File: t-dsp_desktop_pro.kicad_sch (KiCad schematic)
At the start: 192 parts, among them IC1 Logic Level Shifter - 74HCT2G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, J1 jumper, J10 JST-XH Connector -, J11 JST-XH Connector -, J12 RGB LED HEADEER, J13 Conn_01x02, J14 Conn_01x03, J15 Conn_01x01, J16 Conn_01x02, J17 Conn_02x04_Odd_Even, J18 Conn_02x02_Odd_Even, J19 Conn_01x01, J2 GROUND HEADER, J20 Conn_01x01, J3 jumper, J4 jumper, J5 jumper, J6 jumper, J7 jumper, J8 PJRAS2X1S01X, J9 PJRAS2X1S01X, Q1 DMG2307L-7, Q2 DMG2307L-7, SW1 SW_SPST, SW2 TL1105WF160Q - 3.15mm actuator, SW3 SW_SPST, SW4 SW_SPST, SW5 RotaryEncoder_Switch_MP, SW6 TL1105WF160Q - 3.15mm actuator, SW7 TL1105WF160Q - 3.15mm actuator, SW8 TL1105WF160Q - 3.15mm actuator, T108 Tab, T109 Tab, T110 Tab, T111 Tab, U1 Teensy 4.1 - DEVKIT, U10 TPD4E02B04DQA, U2 ESP32-DevKitC - DEVKIT, U3 Power Mux & Protect - TPS2116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, U4 Optoisolators - H11L1SM - 6-S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, U5 Dual Buffer - SN74LVC2G125DCTR, U6 Dual Buffer - SN74LVC2G125DCTR, U7 Dual Buffer - SN74LVC2G125DCTR, U8 Dual Buffer - SN74LVC2G125DCTR, U9 Dual Buffer - 74HCT2G17GW,125

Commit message: v0.81: Fix CI release, localize 3D models, update README with render gallery
- Fix workflow: add gh release create before upload (tag != release)
- Fix ZIP filename: remove empty %r board revision from output name
- Localize 3D model paths for U10, C15, JST connectors to ${KIPRJMOD}
- Add project-local footprints for C_1206 and JST_XH_S2B-XH-A
- Trim SMD 3D renders from 8 to 4 views (top, bottom, top_iso, bottom_iso)
- Update gallery.html to handle different view counts per set
- Update README: Blender render thumbnails linking to gallery, fix IC table,
  add new components (U10, IC1, D5, Q1/Q2), update project files table
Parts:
- C1, C29, C30: Digikey 13-CC1206MKX5R5BB107CT-ND -> (none); Manufacturer YAGEO -> (none); Manufacturer_Part_Number CC1206MKX5R5BB107 -> (none)
- C10, C11, C2, C22, C24, C25, C26, C3, C4, C5: Manufacturer Kyocera AVX -> (none); Manufacturer_Part_Number 08055C104M4T4A -> (none)
- C15: footprint Capacitor_SMD:C_1206_3216Metric_Pad1.33x1.80mm_HandSolder -> project_fp:C_1206_3216Metric_Pad1.33x1.80mm_HandSolder
- C16, C17, C18, C19, C20, C21: Manufacturer KEMET -> (none); Manufacturer_Part_Number C0805C104K5RAC7411 -> (none)
- CC1, CC2, R29, R30: Digikey - -> (none); Manufacturer - -> (none); Manufacturer_Part_Number 0805W8F5101T5E -> (none)
- D2: Manufacturer Panjit -> (none); Manufacturer_Part_Number 1N4148W_R1_00001 -> (none)
- D5: LCSC TYPE (none) -> SMD; Manufacturer_Name Texas Instruments -> (none); Manufacturer_Part_Number TPD1E10B06DPYT -> (none); Mouser Part Number 595-TPD1E10B06DPYT -> (none); Mouser Price/Stock https://www.mouser.co.uk/ProductDetail/Texas-Instruments/TP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 -> (none)
- ESP_I1, MIDI_IO1, TDM1, TDM2, USB_DEVICE_1, USB_HOST_1: Digikey - -> (none); Manufacturer - -> (none); Manufacturer_Part_Number - -> (none)
- G1, G2, ILI_LED1, ILI_LED2, J1, J3, J4, J5, J6, J7, MIDI_OT1, MIDI_OT2: Digikey - -> (none); Manufacturer - -> (none); Manufacturer_Part_Number ~jumper -> (none)
- HPTRS1, HPTRS2: Manufacturer Switchcraft -> (none); Manufacturer_Part_Number 35RAPC3BH3 -> (none)
- IC1: Manufacturer_Name Nexperia -> (none); Manufacturer_Part_Number 74HCT2G125DC,125 -> (none)
- J10, J11: value JST-XH Connector - -> JST-XH Connector; footprint Connector_JST:JST_XH_S2B-XH-A_1x02_P2.50mm_Horizontal -> project_fp:JST_XH_S2B-XH-A_1x02_P2.50mm_Horizontal; Manufacturer_Part_Number JST-XH -> (none)
- MIDI_IN_1, MIDI_OUT_1: Manufacturer Switchcraft -> (none); Manufacturer_Part_Number 35RAPC4BHN2 -> (none)
- PU_EN108: TAC5212EVM n/a -> (none)
- PWR1, PWR2, PWR3: Manufacturer_Part_Number through-hole -> (none)
- Q1, Q2: Manufacturer_Name Diodes Incorporated -> (none); Manufacturer_Part_Number DMG2307L-7 -> (none); Mouser Part Number 621-DMG2307L-7 -> (none); Mouser Price/Stock https://www.mouser.co.uk/ProductDetail/Diodes-Incorporated/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 -> (none); Package / Case (none) -> SOT-23
- R11, R20, R21: Digikey ERJ-PA2F2211X-ND -> (none); Manufacturer YAGEO -> (none); Manufacturer_Part_Number RC0805DR-072K2L -> (none)
- R28: Digikey - -> (none); Manufacturer - -> (none); Manufacturer_Part_Number ERJ-PB6D5101V -> (none)
- R32, R34, R36, R37, R38, R39: Manufacturer Bourns -> (none); Manufacturer_Part_Number CR0805-FX-2200ELF -> (none)
- R33: Manufacturer Panasonic -> (none); Manufacturer_Part_Number ERA-6AED152V -> (none)
- TR1: Manufacturer Everlight Electronics -> (none); Manufacturer_Part_Number FCR6842032R -> (none)
- TT1: Manufacturer Everlight Electronics -> (none); Manufacturer_Part_Number FCR6842032T -> (none)
- U1: Manufacturer PJRC -> (none); Manufacturer_Part_Number ~Teensy4.1 -> (none)
- U10: footprint Package_SON:USON-10_2.5x1.0mm_P0.5mm -> project_fp:TPD4E02B04DQA; LCSC TYPE (none) -> SMD
- U4: Manufacturer_Part_Number H11L1SM -> (none)
- U9: Manufacturer_Part_Number 74HCT2G17GW,125 -> (none)
- USBA1: Digikey 380-1412-ND -> (none); Manufacturer Stewart Connector -> (none); Manufacturer_Part_Number SS-52100-001 -> (none)
- board_outline2: Digikey - -> (none); Manufacturer - -> (none); Manufacturer_Part_Number ~BOARD -> (none)

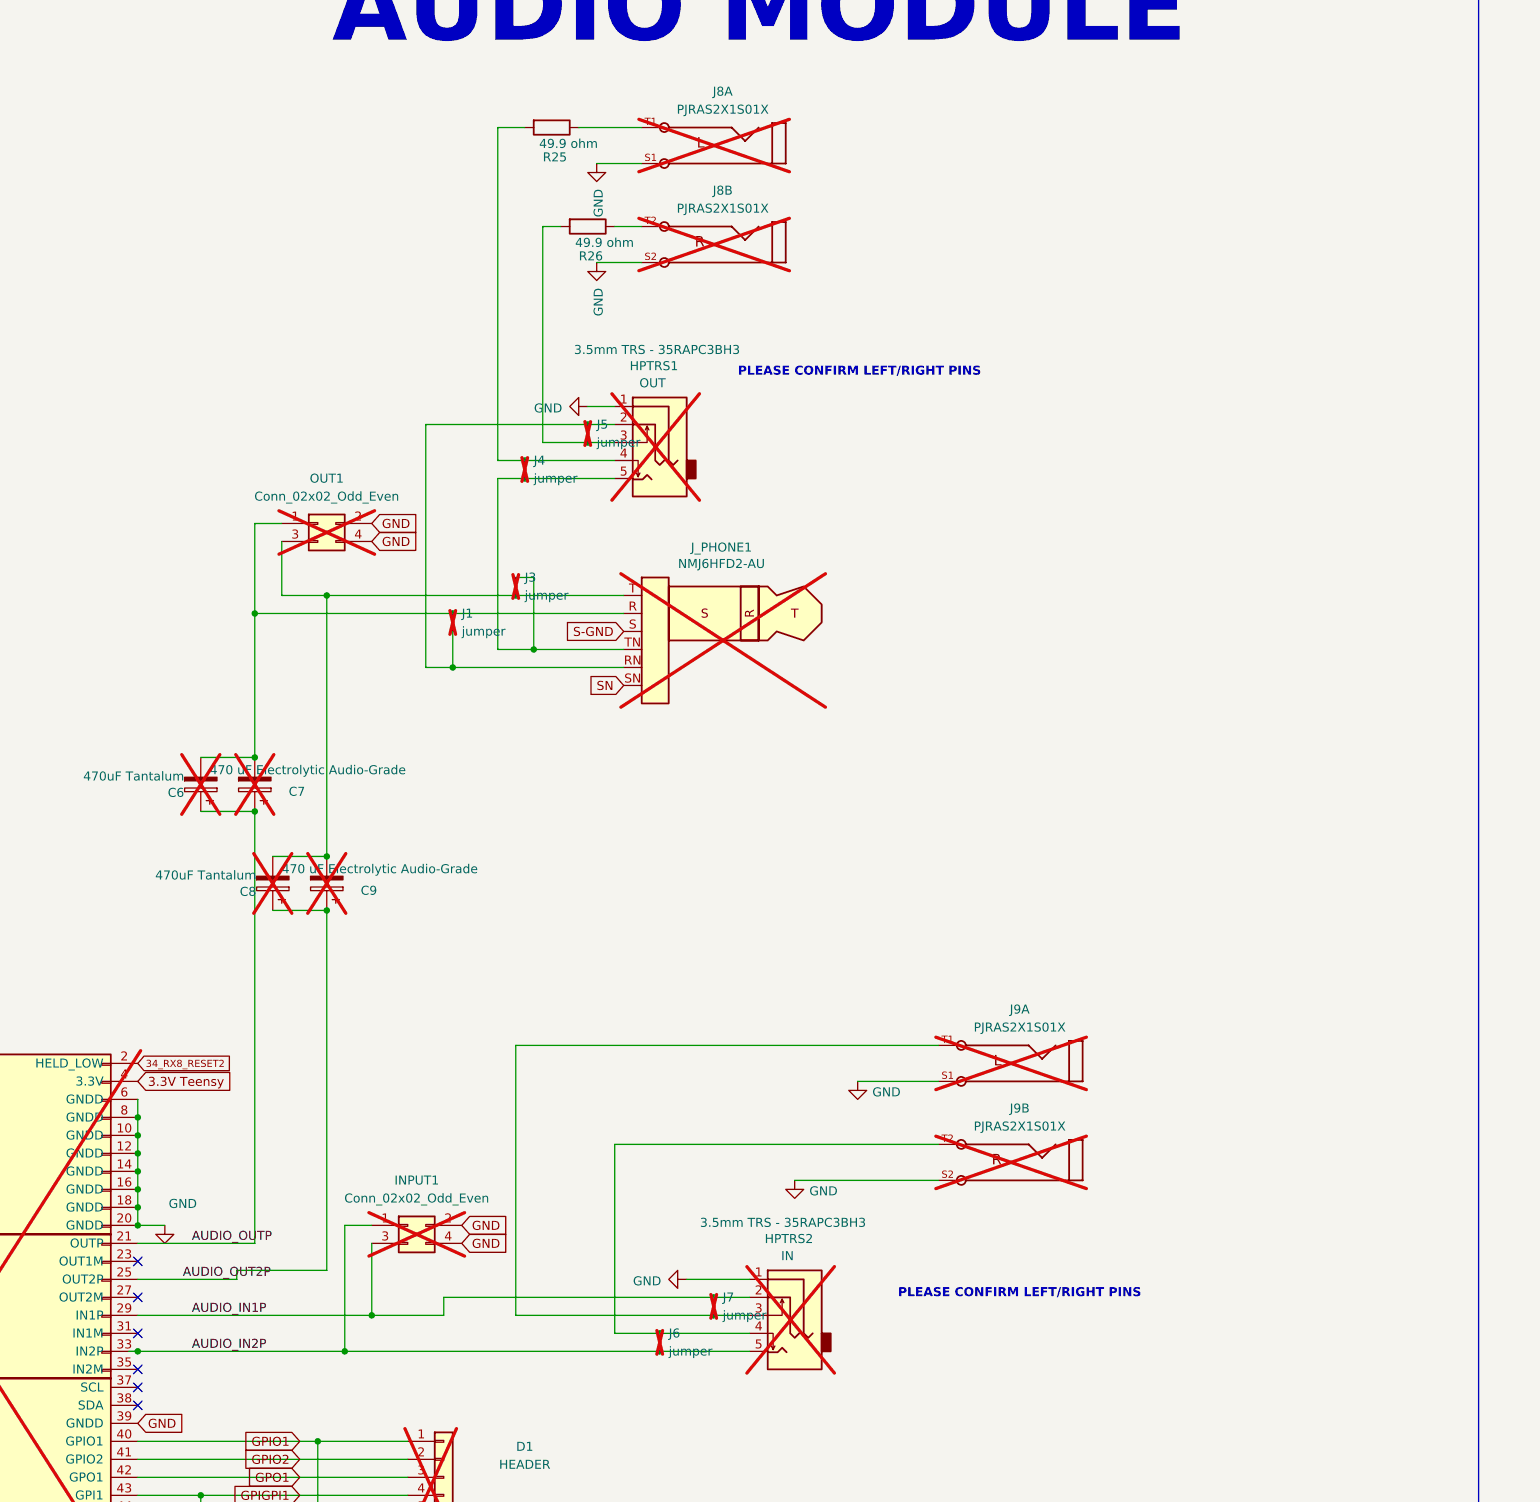
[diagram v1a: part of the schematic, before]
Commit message: v0.82: Fix audio output pin mapping and add PTC fuse footprint
- Correct L/R channel assignment: Left=OUT1, Right=OUT2
- Fix tip/ring polarity: +=tip, -=ring
- Add PTC resettable fuse (MF-LSMF300) footprint and 3D model
- Update workflow to include tag in manufacturing ZIP filename
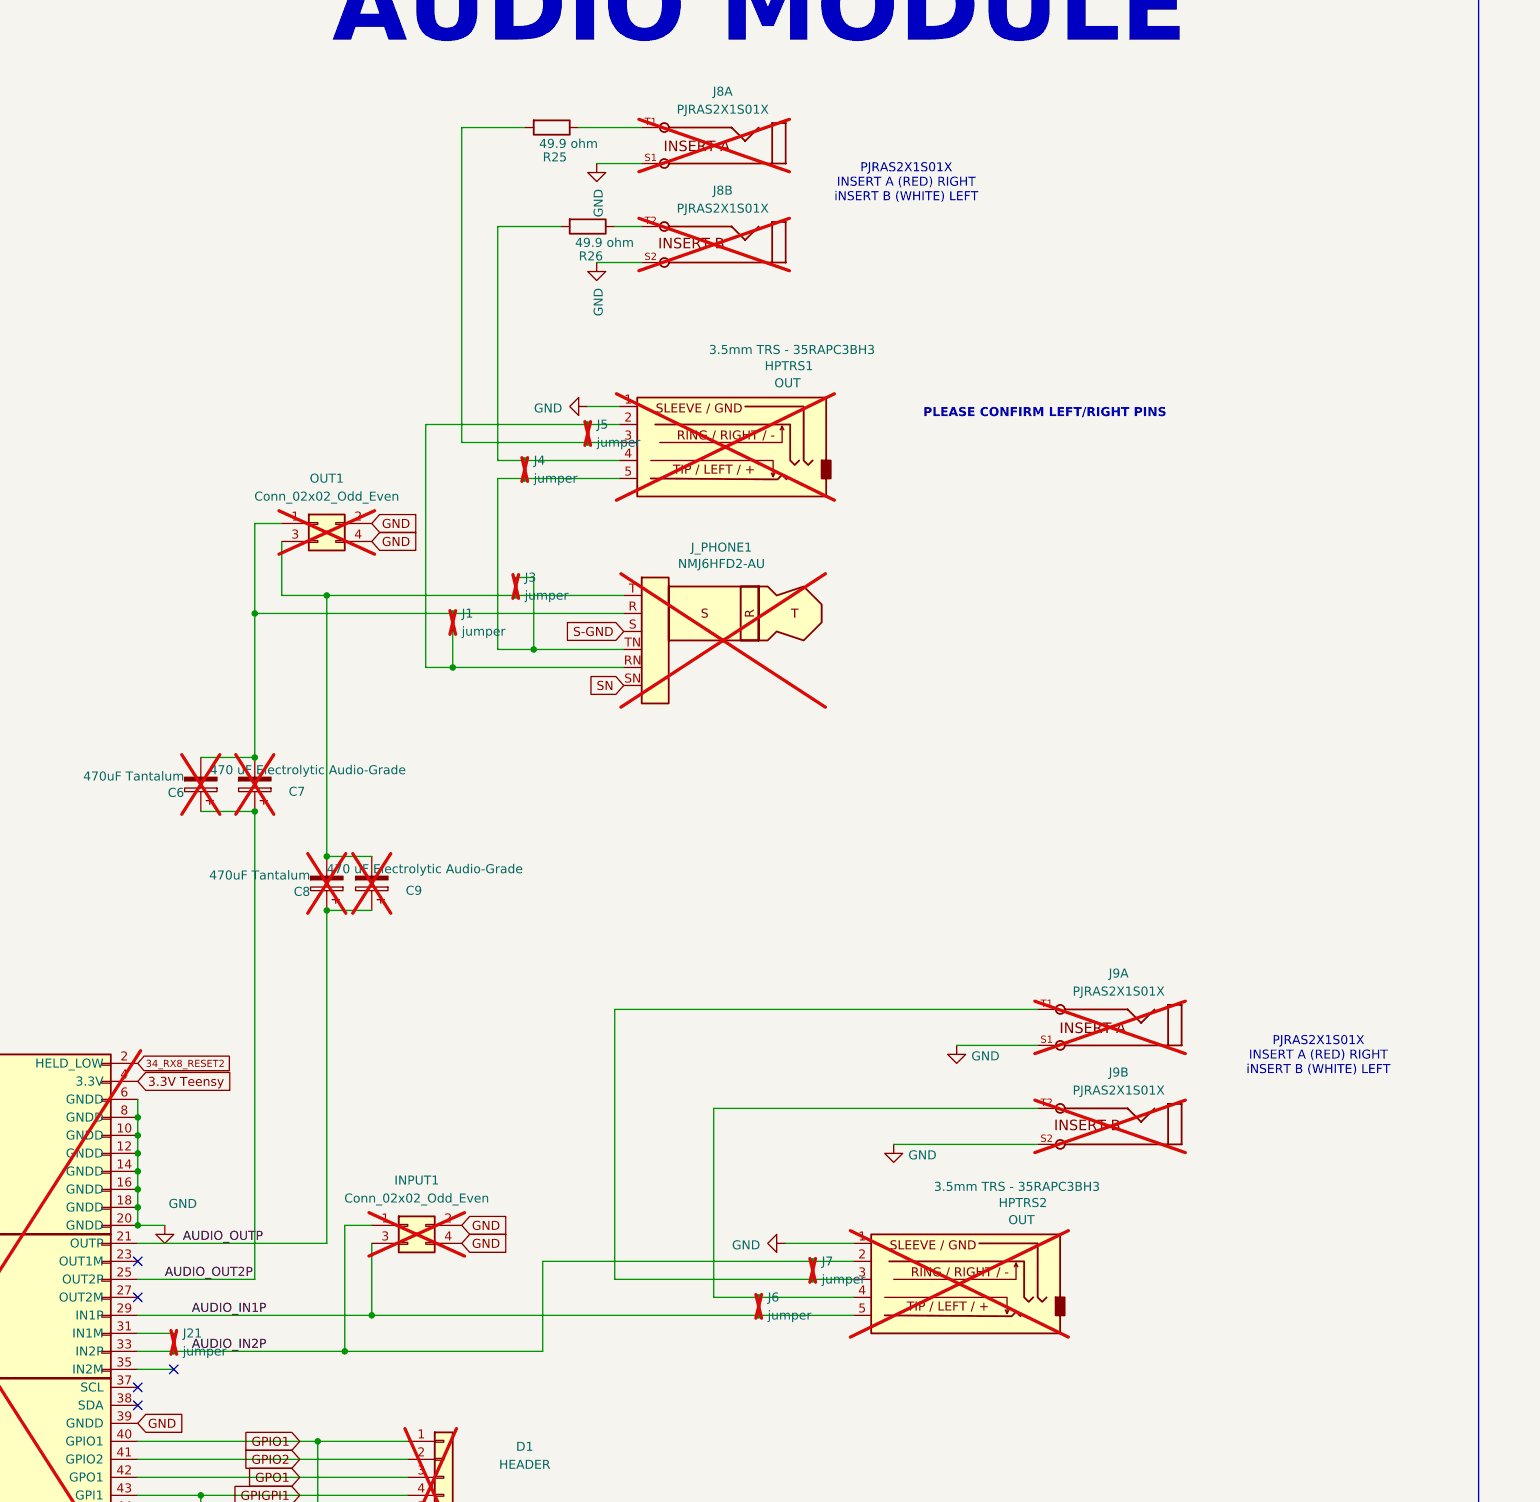
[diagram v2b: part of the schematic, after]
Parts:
- added J21: jumper, project_fp:jumper_slice, symbol project_sch:NetTie_2_mod
- HPTRS1: Manufacturer (none) -> Switchcraft; Manufacturer_Part_Number (none) -> 35RAPC3BH3
- HPTRS2: Label IN -> OUT; Manufacturer (none) -> Switchcraft; Manufacturer_Part_Number (none) -> 35RAPC3BH3
- J8, J9: Availability (none) -> In Stock; Check_prices (none) -> https://www.snapeda.com/parts/PJRAS2X1S01X/SWITCHCRAFT/view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; Description_1 (none) -> Connector, 2POS RA SHLD PHJK RE | Switchcraft PJRAS2X1S01X; MANUFACTURER (none) -> Switchcraft; MF (none) -> Switchcraft Inc.; MP (none) -> PJRAS2X1S01X; Package (none) -> None; Price (none) -> None; SnapEDA_Link (none) -> https://www.snapeda.com/parts/PJRAS2X1S01X/SWITCHCRAFT/view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
- J9: footprint project_fp:PJRAS2X1S01X_MOD2 -> PJRAS2X1S01X:PJRAS2X1S01X; Availability (none) -> In Stock; Check_prices (none) -> https://www.snapeda.com/parts/PJRAS2X1S01X/SWITCHCRAFT/view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; Description_1 (none) -> Connector, 2POS RA SHLD PHJK RE | Switchcraft PJRAS2X1S01X; MANUFACTURER (none) -> Switchcraft; MF (none) -> Switchcraft Inc.; MP (none) -> PJRAS2X1S01X; Package (none) -> None; Price (none) -> None; SnapEDA_Link (none) -> https://www.snapeda.com/parts/PJRAS2X1S01X/SWITCHCRAFT/view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
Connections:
- net AUDIO_IN1P: now also HPTRS2.5, J6.1; no longer HPTRS2.2, J7.2
- net AUDIO_IN2P: now also HPTRS2.2, J7.2, J21.1; no longer HPTRS2.5, J6.1
- net AUDIO_OUT2P: now also C6.1, C7.1; no longer C8.1, C9.1
- net AUDIO_OUTP: now also C8.1, C9.1; no longer C6.1, C7.1
- net at HPTRS1.3, J5.1: now also R25.2; no longer R26.2
- net at board_outline1.31 (IN1M): now also J21.2
- net at HPTRS1.4, J4.2: now also R26.2; no longer R25.2
- no-connect marks 19 -> 18
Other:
- note added: "PJRAS2X1S01X INSERT A (RED) RIGHT iNSERT B (WHITE) LEFT"
- moved on the sheet: C8, C9, J6, J7, J9A, J9B
